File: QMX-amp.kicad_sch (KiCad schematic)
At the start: 4 parts, among them J1 RF-IN, J2 RF-OUT, J3 Conn_01x04_Pin, U4 SJ1-3523N

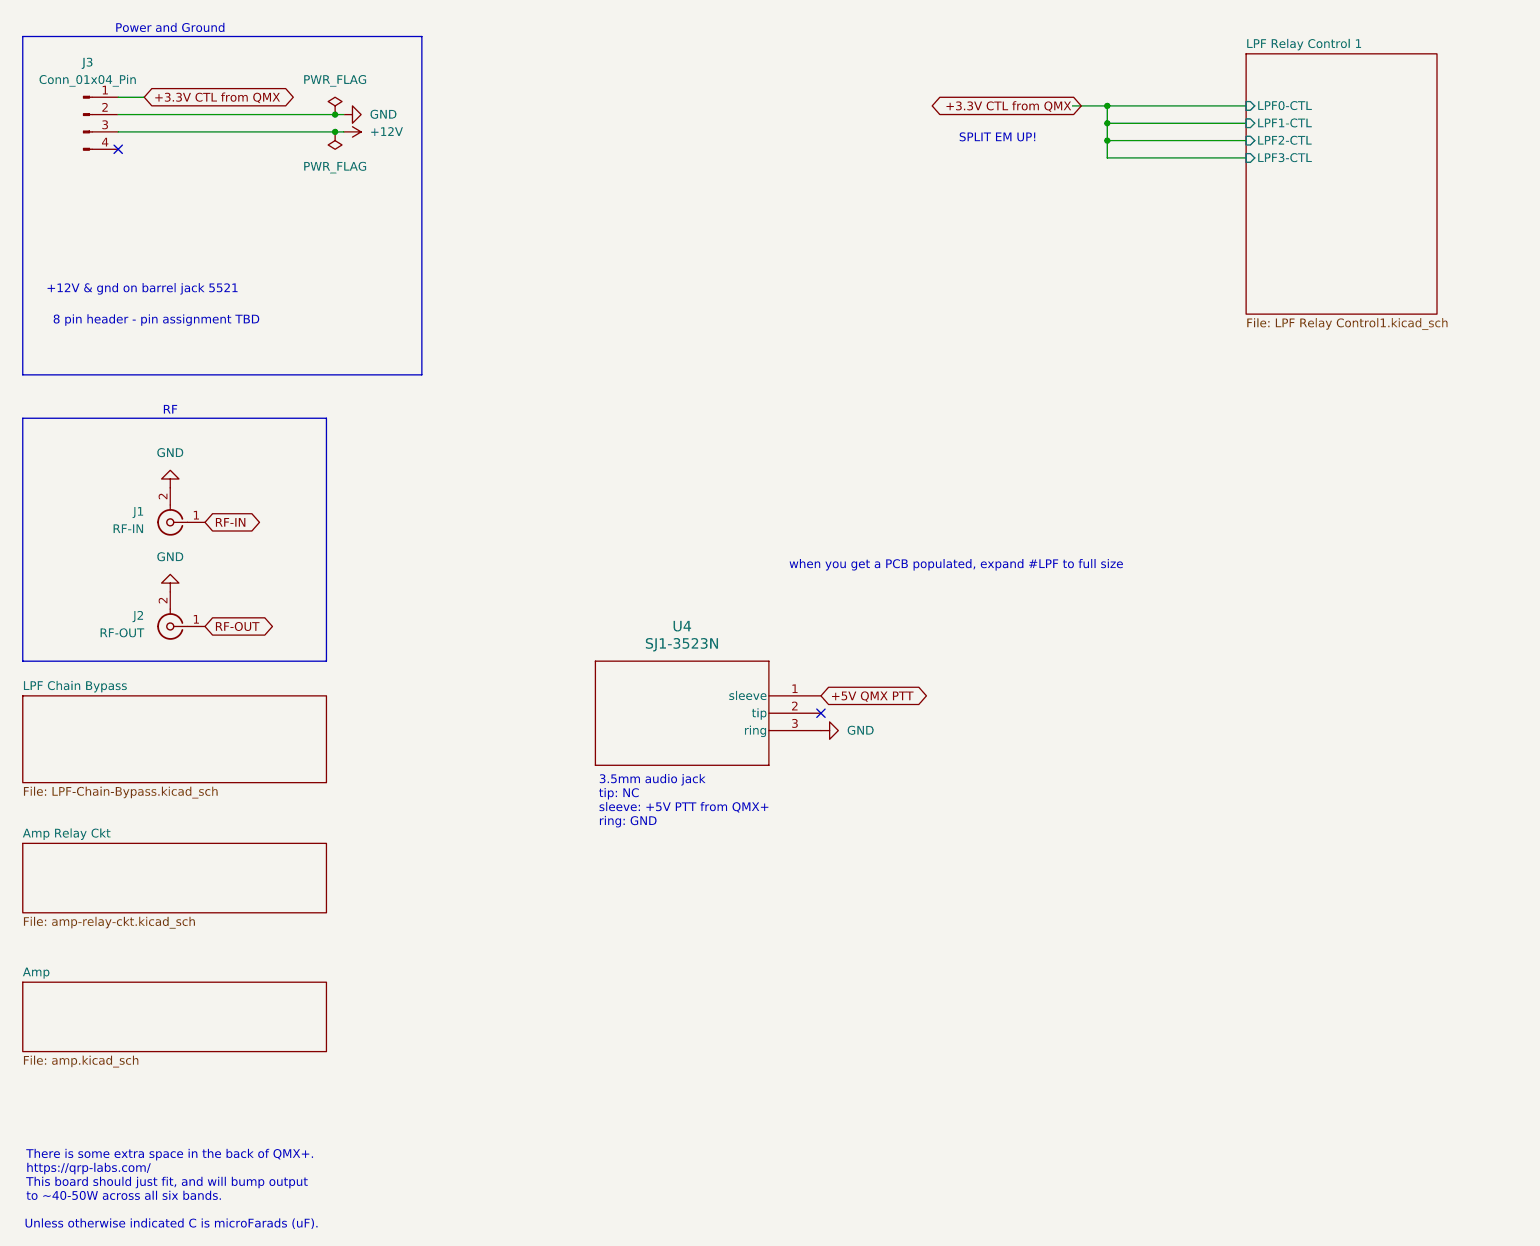
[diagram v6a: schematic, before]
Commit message: expended to all 6 LPFs.  ERC pass.  Need to check component values on new LPF page
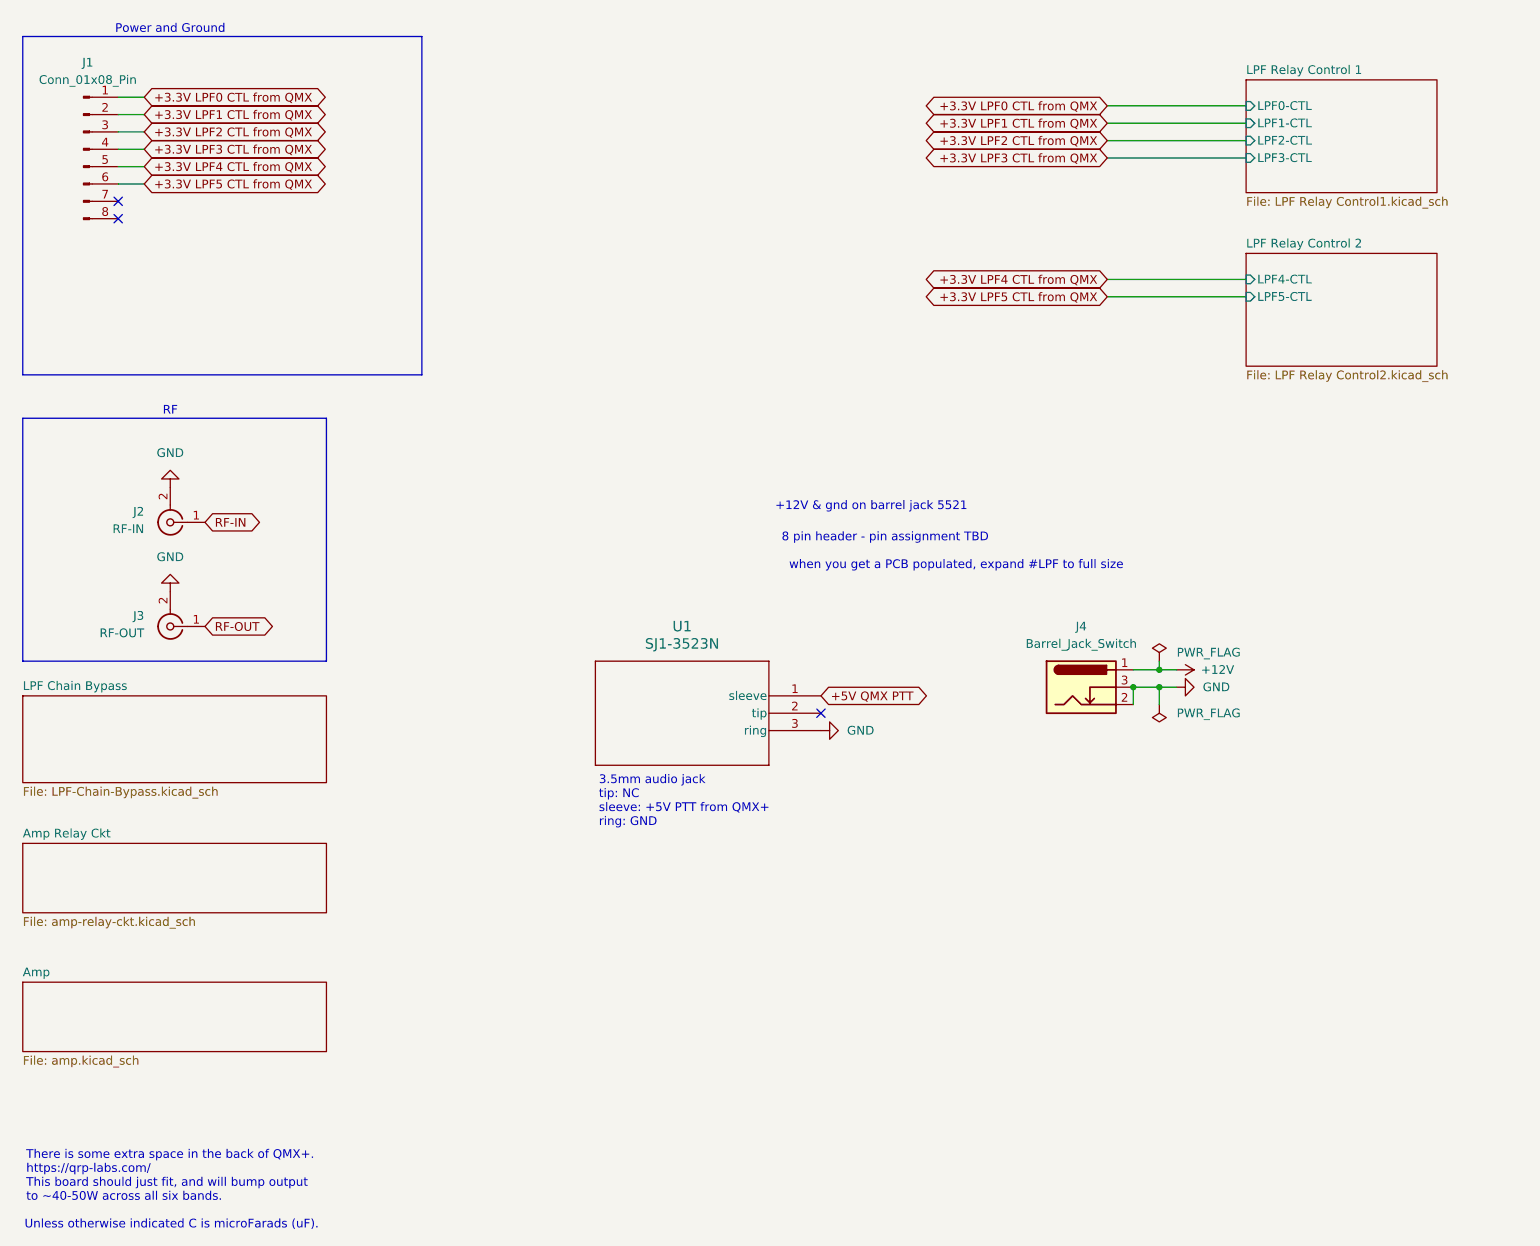
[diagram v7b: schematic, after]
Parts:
- removed J3: Conn_01x04_Pin, symbol Connector:Conn_01x04_Pin
- added J1: Conn_01x08_Pin, symbol Connector:Conn_01x08_Pin
- added J4: Barrel_Jack_Switch, Connector_BarrelJack:BarrelJack_Horizontal, symbol Connector:Barrel_Jack_Switch
- renumbered J1 to J2, J2 to J3, U4 to U1
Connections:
- net +12V: now also J4.1
- net GND: now also J4.2, J4.3
- new net +3.3V LPF0 CTL from QMX: J1.1 (Pin_1)
- new net +3.3V LPF1 CTL from QMX: J1.2 (Pin_2)
- new net +3.3V LPF2 CTL from QMX: J1.3 (Pin_3)
- new net +3.3V LPF3 CTL from QMX: J1.4 (Pin_4)
- new net +3.3V LPF4 CTL from QMX: J1.5 (Pin_5)
- new net +3.3V LPF5 CTL from QMX: J1.6 (Pin_6)
- no-connect marks 2 -> 3
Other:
- added sheet LPF Relay Control 2 (LPF Relay Control2.kicad_sch)
- note removed: "SPLIT EM UP!"

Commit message: v0.9 ERC passes.  All parts have footprints.  Need to renumber pages so things related are closer in printout
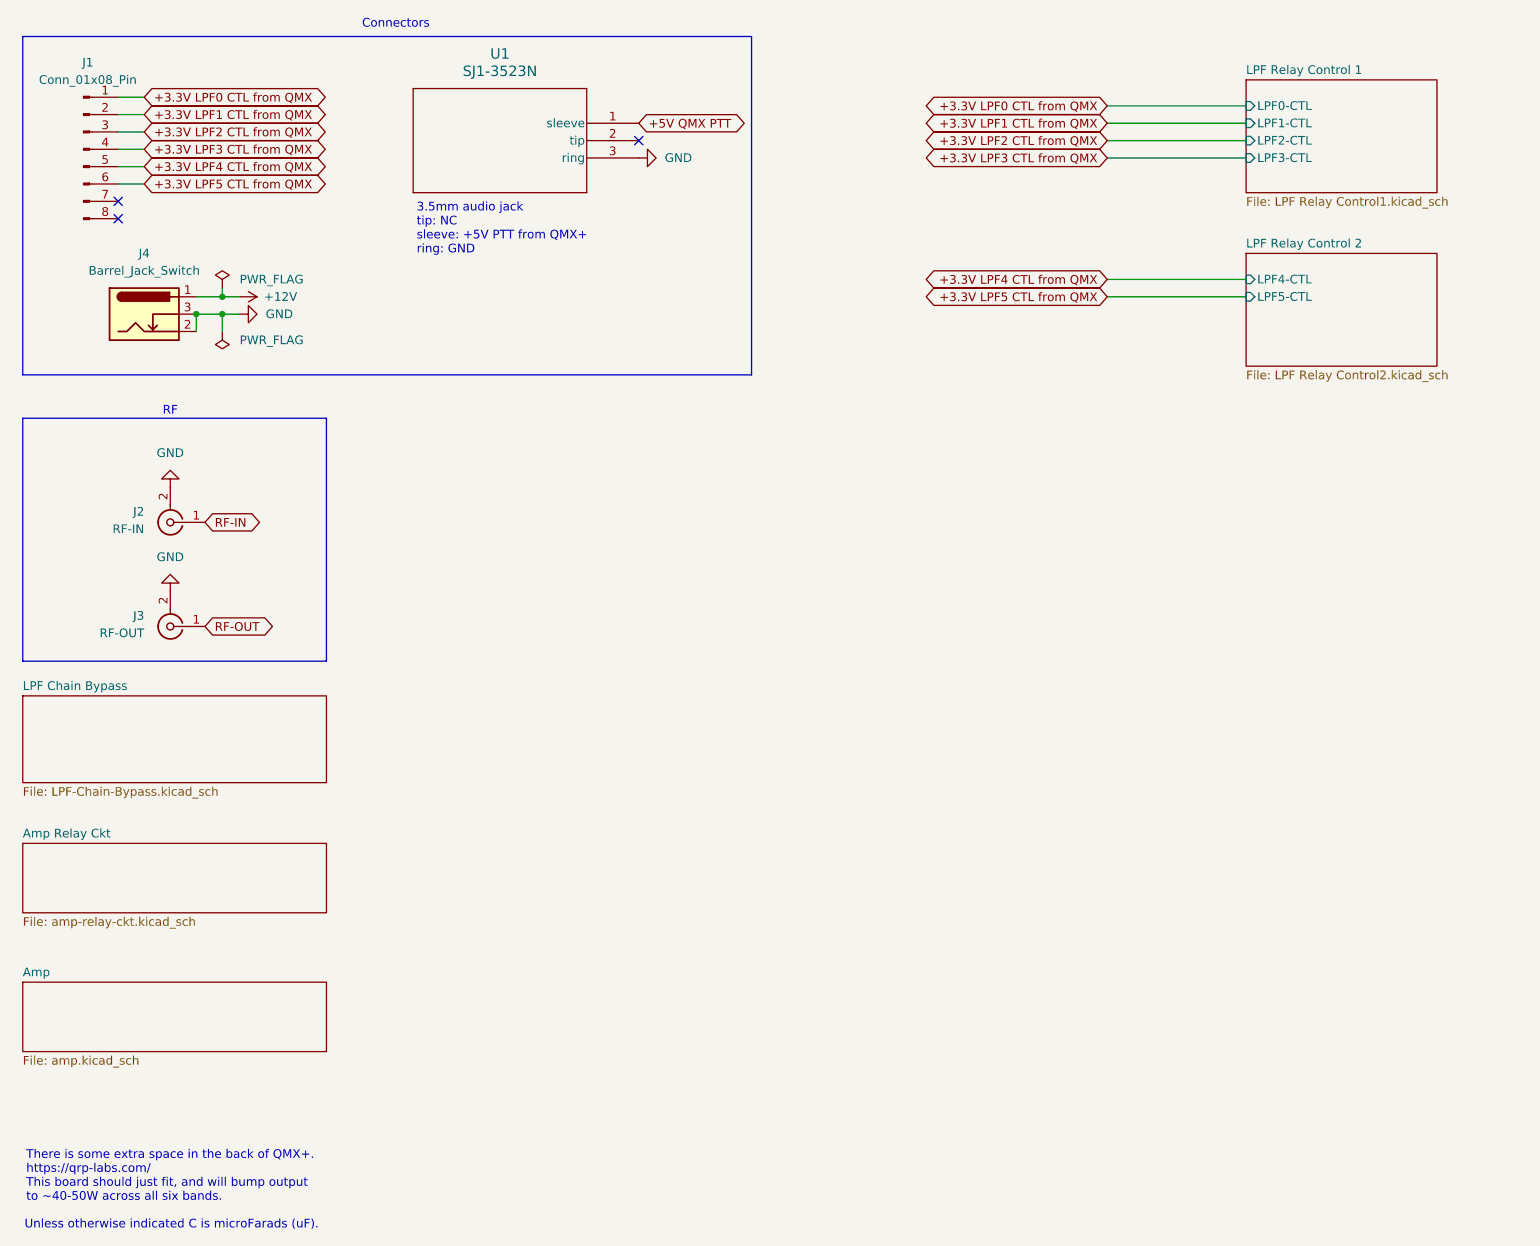
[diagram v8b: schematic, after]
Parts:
- J1: footprint (none) -> Connector_PinHeader_1.00mm:PinHeader_1x08_P1.00mm_Horizontal
- J2, J3: footprint (none) -> Connector_Coaxial:BNC_Amphenol_B6252HB-NPP3G-50_Horizontal
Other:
- note added: "Connectors"
- note removed: "+12V & gnd on barrel jack 5521"
- note removed: "8 pin header - pin assignment TBD"
- note removed: "Power and Ground"
- note removed: "when you get a PCB populated, expand #LPF to full size"
- moved on the sheet: J4, U1
